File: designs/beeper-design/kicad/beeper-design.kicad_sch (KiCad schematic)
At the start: 90 parts, among them J1 TC2030-IDC-NL, J2 TC2030-IDC-NL, J3 2X1-pin-header, J4 2X1-pin-header, J5 6X1-pin-header, U1 DA14705-00000HZ2, U10 PMM-3738-VM1000-R, U11 LI0805H151R-10, U12 DRV2605YZFR, U13 CSD75207W15, U14 EVPBB4A9B000, U15 EVPBB4A9B000, U16 EVPBB4A9B000, U2 AT25FF321A-UUN-T, U3 BQ51003YFPR, U4 DA7212-01UM2, U5 PMM-3738-VM1000-R, U6 LI0805H151R-10, U7 PMM-3738-VM1000-R, U8 LI0805H151R-10, U9 LSM6DSOXTR, X1 ABM12-32.000MHZ-B2X-T3

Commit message: fixed BGA ball landpattern
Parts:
- removed C10: 2.2u, beeper-design:Pkg0201_4, symbol my_capacitor_35
- removed C11: 10u, beeper-design:Pkg0402_1, symbol my_capacitor
- removed C12: 10u, beeper-design:Pkg0402_1, symbol my_capacitor_18
- removed C13: 1u, beeper-design:Pkg0201_4, symbol my_capacitor_4
- removed C14: 2.2u, beeper-design:Pkg0201_4, symbol my_capacitor_33
- removed C15: 470n, beeper-design:Pkg0201_4, symbol my_capacitor_37
- removed C16: 470n, beeper-design:Pkg0201_4, symbol my_capacitor_41
- removed C17: 22n, beeper-design:Pkg0201_1, symbol my_capacitor_3
- removed C18: 22n, beeper-design:Pkg0201_1, symbol my_capacitor_6
- removed C19: 10n, beeper-design:Pkg0201_1, symbol my_capacitor_10
- removed C2: 22u, beeper-design:Pkg0603, symbol my_capacitor_24
- removed C20: 10n, beeper-design:Pkg0201_1, symbol my_capacitor_16
- removed C21: 270p, beeper-design:Pkg0201_1, symbol my_capacitor_20
- removed C22: 10n, beeper-design:Pkg0201_1, symbol my_capacitor_25
- removed C23: 10u, beeper-design:Pkg0402_1, symbol my_capacitor_36
- removed C24: 4.7u, beeper-design:Pkg0402_2, symbol my_capacitor_40
- removed C25: 4.7u, beeper-design:Pkg0402_2, symbol my_capacitor_29
- removed C26: 1u, beeper-design:Pkg0201_4, symbol my_capacitor_26
- removed C27: 100n, beeper-design:Pkg0201_1, symbol my_capacitor_34
- removed C28: 1u, beeper-design:Pkg0201_4, symbol my_capacitor_39
- removed C29: 1u, beeper-design:Pkg0201_4, symbol my_capacitor_1
- removed C3: 22u, beeper-design:Pkg0603, symbol my_capacitor_32
- removed C30: 1u, beeper-design:Pkg0201_4, symbol my_capacitor_5
- removed C31: 1u, beeper-design:Pkg0201_4, symbol my_capacitor_7
- removed C32: 1u, beeper-design:Pkg0201_4, symbol my_capacitor_11
- removed C33: 1u, beeper-design:Pkg0201_4, symbol my_capacitor_17
- removed C34: 1u, beeper-design:Pkg0201_4, symbol my_capacitor_22
- removed C35: 1u, beeper-design:Pkg0201_4, symbol my_capacitor_28
- removed C36, C39, C44: 1u, beeper-design:Pkg0201_4, symbol my_capacitor_13
- removed C37, C40, C45: 100p, beeper-design:Pkg0201_1, symbol my_capacitor_19
- removed C38, C41, C46: 1u, beeper-design:Pkg0201_4, symbol my_capacitor_31
- removed C4: 47u, beeper-design:Pkg0805_1, symbol my_capacitor_38
- removed C42: 100n, beeper-design:Pkg0201_1, symbol my_capacitor_9
- removed C43: 100n, beeper-design:Pkg0201_1, symbol my_capacitor_14
- removed C47: 1u, beeper-design:Pkg0201_4, symbol my_capacitor_23
- removed C48: 1u, beeper-design:Pkg0201_4, symbol my_capacitor_30
- removed C5: 100n, beeper-design:Pkg0201_1, symbol my_capacitor_2
- removed C6: 47u, beeper-design:Pkg0805_1, symbol my_capacitor_8
- removed C7: 10u, beeper-design:Pkg0402_1, symbol my_capacitor_12
- removed C8: 10u, beeper-design:Pkg0402_1, symbol my_capacitor_21
- removed C9: 10u, beeper-design:Pkg0402_1, symbol my_capacitor_27
- removed J1, J2: TC2030-IDC-NL, beeper-design:TC2030_IDC_NL_FOOTPRINT, symbol component_1
- removed J3, J4: 2X1-pin-header, beeper-design:PIN_GRID_1, symbol pin_header
- removed J5: 6X1-pin-header, beeper-design:PIN_GRID, symbol pin_header_1
- removed R1: 0R, beeper-design:Pkg0201_5, symbol my_resistor_9
- removed R10, R11, R9: 47K, beeper-design:Pkg0201_5, symbol my_resistor_7
- removed R12, R13: 8K2, beeper-design:Pkg0201_5, symbol my_resistor_1
- removed R14, R15: 8K2, beeper-design:Pkg0201_5, symbol my_resistor_5
- removed R16, R17: 8K2, beeper-design:Pkg0201_5, symbol my_resistor_11
- removed R2: 845R, beeper-design:Pkg0201_5, symbol my_resistor_10
- removed R3: 196R, beeper-design:Pkg0201, symbol my_resistor
- removed R4: 20K, beeper-design:Pkg0201_3, symbol my_resistor_2
- removed R5: 10K, beeper-design:Pkg0201_5, symbol my_resistor_3
- removed R6: 10K, beeper-design:Pkg0201_5, symbol my_resistor_4
- removed R7: 10K, beeper-design:Pkg0201_5, symbol my_resistor_6
- removed R8: 1K, beeper-design:Pkg0201, symbol my_resistor_8
- removed U10, U5, U7: PMM-3738-VM1000-R, beeper-design:LP_7, symbol PMM_3738_VM1000_R
- removed U11, U6, U8: LI0805H151R-10, beeper-design:Pkg0805, symbol component
- removed U4: DA7212-01UM2, beeper-design:LP_2, symbol component_2
- removed X1: ABM12-32.000MHZ-B2X-T3, beeper-design:XTAL_TSX_3225, symbol component_3
- added C10: 2.2u, beeper-design:Pkg0201_4, symbol my_capacitor_32
- added C11: 10u, beeper-design:Pkg0402_1, symbol my_capacitor_38
- added C12: 10u, beeper-design:Pkg0402_1, symbol my_capacitor_19
- added C13: 1u, beeper-design:Pkg0201_4, symbol my_capacitor_24
- added C14: 2.2u, beeper-design:Pkg0201_4, symbol my_capacitor_8
- added C15: 470n, beeper-design:Pkg0201_4, symbol my_capacitor_12
- added C16: 470n, beeper-design:Pkg0201_4, symbol my_capacitor_18
- added C17: 22n, beeper-design:Pkg0201_1, symbol my_capacitor_23
- added C18: 22n, beeper-design:Pkg0201_1, symbol my_capacitor_29
- added C19: 10n, beeper-design:Pkg0201_1, symbol my_capacitor_33
- added C2: 22u, beeper-design:Pkg0603, symbol my_capacitor_27
- added C20: 10n, beeper-design:Pkg0201_1, symbol my_capacitor_37
- added C21: 270p, beeper-design:Pkg0201_1, symbol my_capacitor_1
- added C22: 10n, beeper-design:Pkg0201_1, symbol my_capacitor_3
- added C23: 10u, beeper-design:Pkg0402_1, symbol my_capacitor_10
- added C24: 4.7u, beeper-design:Pkg0402_2, symbol my_capacitor_16
- added C25: 4.7u, beeper-design:Pkg0402_2, symbol my_capacitor_6
- added C26: 1u, beeper-design:Pkg0201_4, symbol my_capacitor_4
- added C27: 100n, beeper-design:Pkg0201_1, symbol my_capacitor_9
- added C28: 1u, beeper-design:Pkg0201_4, symbol my_capacitor_14
- added C29: 1u, beeper-design:Pkg0201_4, symbol my_capacitor_20
- added C3: 22u, beeper-design:Pkg0603, symbol my_capacitor_31
- added C30: 1u, beeper-design:Pkg0201_4, symbol my_capacitor_25
- added C31: 1u, beeper-design:Pkg0201_4, symbol my_capacitor_30
- added C32: 1u, beeper-design:Pkg0201_4, symbol my_capacitor_34
- added C33: 1u, beeper-design:Pkg0201_4, symbol my_capacitor_39
- added C34: 1u, beeper-design:Pkg0201_4, symbol my_capacitor_2
- added C35: 1u, beeper-design:Pkg0201_4, symbol my_capacitor_5
- added C36: 100n, beeper-design:Pkg0201_1, symbol my_capacitor_40
- added C4: 47u, beeper-design:Pkg0805, symbol my_capacitor_35
- added C42: 100n, beeper-design:Pkg0201_1, symbol my_capacitor_21
- added C43: 100n, beeper-design:Pkg0201_1, symbol my_capacitor_26
- added C47: 1u, beeper-design:Pkg0201_4, symbol my_capacitor_11
- added C48: 1u, beeper-design:Pkg0201_4, symbol my_capacitor_17
- added C49: 1p, beeper-design:Pkg0201_1, symbol my_capacitor_36
- added C5: 100n, beeper-design:Pkg0201_1, symbol my_capacitor
- added C50: 1p, beeper-design:Pkg0201_1, symbol my_capacitor_41
- added C6: 47u, beeper-design:Pkg0805, symbol my_capacitor_7
- added C7: 10u, beeper-design:Pkg0402_1, symbol my_capacitor_13
- added C8: 10u, beeper-design:Pkg0402_1, symbol my_capacitor_22
- added C9: 10u, beeper-design:Pkg0402_1, symbol my_capacitor_28
- added F1: TPD4S012DRYR, beeper-design:SON_6_L1_5_W1_0_P0_50_BL, symbol C96506
- added J1: TC2030-IDC-NL, beeper-design:TC2030_IDC_NL_FOOTPRINT, symbol component_2
- added J3, J4: 2X1-pin-header, beeper-design:PIN_GRID_1, symbol pin_header_1
- added J5: 6X1-pin-header, beeper-design:PIN_GRID, symbol pin_header
- added J6: 10103594-0001LF, beeper-design:AMPHENOL_10103594_0001LF, symbol AMPHENOL_10103594_0001LF
- added L3: 1n, beeper-design:Pkg0201_2, symbol my_inductor_2
- added R1: 0R, beeper-design:Pkg0201_5, symbol my_resistor_8
- added R12, R13: 8K2, beeper-design:Pkg0201_5, symbol my_resistor_7
- added R14, R15: 8K2, beeper-design:Pkg0201_5, symbol my_resistor_2
- added R16, R17: 8K2, beeper-design:Pkg0201_5, symbol my_resistor_5
- added R18: 100K, beeper-design:Pkg0201_5, symbol my_resistor_10
- added R2: 845R, beeper-design:Pkg0201_5, symbol my_resistor_3
- added R3: 196R, beeper-design:Pkg0201, symbol my_resistor_4
- added R4: 20K, beeper-design:Pkg0201_3, symbol my_resistor_6
- added R5: 10K, beeper-design:Pkg0201_5, symbol my_resistor_9
- added R6: 10K, beeper-design:Pkg0201_5, symbol my_resistor_11
- added R7: 10K, beeper-design:Pkg0201_5, symbol my_resistor
- added R8: 1K, beeper-design:Pkg0201, symbol my_resistor_1
- added U17: (no value), beeper-design:Pkg_2450AT18D0100_STD_R_1, symbol component_1
- added U4: DA7212-01UM2, beeper-design:LP, symbol component
- added XTAL1: XRCGB32M000F1H00R0, beeper-design:CRYSTAL_SMD_4P_L2_0_W1_6_BL_1, symbol C880116
- U1: footprint beeper-design:LP_1 -> beeper-design:LP_5
- U12: footprint beeper-design:LP_5 -> beeper-design:LP_6
- U14, U15, U16: footprint beeper-design:LP_6 -> beeper-design:LP_2
- U9: footprint beeper-design:LP -> beeper-design:LP_1
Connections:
- net GND: now also C10.1, C11.1, C12.1, C13.1, C14.1, C2.1, C23.1, C24.1, C25.1, C26.1, C27.1, C28.1, C29.1, C3.1, C30.1, C31.1, C32.1, C33.1, C34.1, C36.2, C4.1, C42.1, C43.1, C47.1, C48.1, C49.2, C5.1, C50.2, C6.1, C7.1, C8.1, C9.1, F1.4 (GND), J1.5, J5.6, J6.5 (GND), R18.2, R3.2, R5.2, R6.2, R7.2, R8.2, U17.0 (GND), U17.2 (GND), U17.3 (GND), U4.B10 (GND_A), U4.B2 (GND_CP), XTAL1.2 (GND1), XTAL1.4 (GND0)
- net OUT+: now also J4.1
- net OUT-: now also J4.2
- net VDD1P4: now also C2.2, C3.2
- net VDD1P8: now also C26.2, C28.2, C32.2, C4.2, C42.2, C43.2, U4.B14 (VDD_MIC), U4.B6 (VDD_A), U4.D10 (VDD_IO)
- net VDD1P8F: now also C5.2, R1.1
- net VDD1P8P: now also C6.2, R1.2
- net VDD3P0: now also C7.2
- net VDDBAT: now also C8.2
- net VDDBUS: now also C9.2
- net VLED: now also C10.2
- net codec-i2c_sda: now also U1.H12 (P2_08), R12.1, U4.C9 (SDA); no longer U1.D2 (P2_12)
- net drv-i2c_sda: now also U1.A5 (P2_07), R16.1; no longer U1.G1 (P2_11)
- net mcu-but0_gpio: now also U1.B1 (P2_04); no longer U1.H12 (P2_08)
- net mcu-but1_gpio: now also U1.B2 (P2_05); no longer U1.H11 (P2_09)
- net mcu-but2_gpio: now also U1.A4 (P2_06); no longer U1.F1 (P2_10)
- net mcu-hap0_gpio: now also U1.F2 (P1_28); no longer U1.E4 (P2_02)
- net mcu-hap1_gpio: now also U1.D1 (P1_29); no longer U1.E6 (P2_03)
- net mcu-wpwr0_gpio: now also U1.E3 (P2_00), R5.1; no longer U1.B1 (P2_04)
- net mcu-wpwr1_gpio: now also U1.J9 (P2_01), R6.1; no longer U1.B2 (P2_05)
- net mcu-wpwr2_gpio: now also U1.E4 (P2_02); no longer U1.A4 (P2_06)
- net mcu-wpwr3_gpio: now also U1.E6 (P2_03), R7.1; no longer U1.A5 (P2_07)
- net mcu_dbg-m33_swdclk: now also J1.4
- net mcu_mcu-etm_clk: now also J5.1
- net mcu_mcu-etm_data0: now also J5.2
- net mcu_mcu-etm_data1: now also J5.3
- net mcu_mcu-etm_data2: now also J5.4
- net mcu_mcu-etm_data3: now also J5.5
- net at U3.G4 (AD): now also R8.1
- net at U3.B1 (AC2), U3.B2 (AC2): now also C16.1, C18.1, C20.1, C21.1, J3.2
- net at U3.F2 (FOD): now also R2.2, R3.1, R4.1
- net at U3.C2 (RECT), U3.C3 (RECT): now also C23.2, C24.2, R4.2
- net at U3.B3 (AC1), U3.B4 (AC1): now also C15.1, C17.1, C19.1, C21.2, C22.2
- net at U1.A10 (RFIOP): now also C49.1, L3.1
- net at U1.F11 (XTAL32Mp): now also XTAL1.1
- net at U1.F12 (XTAL32Mm): now also XTAL1.3
- net at U3.E4 (COMM1): now also C17.2
- net at U12.A2 (REG): now also C47.2
- net at U3.G1 (ILIM): now also R2.1
- net VBUS: now reaches U13.A1 (G1), U13.A2 (D10), U13.A3 (D11)
- net VBUS: now also C25.2, F1.6 (VBUS), J6.1 (VCC)
- net at U3.E2 (CLAMP2): now also C16.2
- net at U3.C1 (BOOT2): now also C20.2
- net at U3.C4 (BOOT1): now also C19.2
- net at U3.E1 (COMM2): now also C18.2
- net at U3.E3 (CLAMP1): now also C15.2
- net VAD: no longer names the net of U1.M9 (VAD)
- net VSYS renamed VDDSYS
- net VDDSYS: now also C11.2, C12.2, C13.2, C14.2, C29.2, C48.2, J1.1, R12.2, R13.2, R14.2, R15.2, R16.2, R17.2, U4.A11 (VDD_SP)
- net codec-i2c_scl renamed mcu_conn-uart_tx
- net mcu_conn-uart_tx: now also J1.6
- net drv-i2c_scl renamed mcu-hap-i2c_scl
- net mcu-hap-i2c_scl: now also U1.H11 (P2_09), R17.1; no longer U1.D3 (P2_13)
- net mcu-i3c_sda renamed qsen-i3c_sda
- net qsen-i3c_sda: now also R14.1
- net mcu_conn-reset_reset: no longer names the net of U1.B10 (nRST)
- net mcu_dbg-m33_swdio renamed mcu_mcu-dbg-m33_swdio
- net mcu_mcu-dbg-m33_swdio: now also J1.2
- net mcu_dbg-snc_swdclk: no longer names the net of U1.D7 (P0_03)
- net mcu_dbg-snc_swdio: no longer names the net of U1.D8 (P0_02)
- net qsen-i3c_scl renamed mcu-i3c_scl
- net mcu-i3c_scl: now also R15.1
- new net: C22.1, J3.1
- new net: C50.1, L3.2, U17.1
- new net: C33.2, U4.A1 (HPCSP)
- new net: C31.2, U4.A7 (DACREF)
- new net: C30.2, U4.A9 (VMID)
- new net: C35.1, U4.C1 (HPCSN)
- new net: C35.2, U4.C3 (HPCFN)
- new net: C27.2, U4.D12 (VDIG)
- new net: C34.2, U4.D2 (HPCFP)
- new net D+: F1.1 (D+), J6.3 (D+), U1.F1 (P2_10)
- new net D-: F1.2 (D-), J6.2 (D-), U1.G1 (P2_11)
- new net SHIELD: C36.1, J6.10 (SHIELD), J6.11 (SHIELD), J6.13 (SHIELD), J6.14 (SHIELD), J6.6 (SHIELD), J6.7 (SHIELD), J6.8 (SHIELD), J6.9 (SHIELD), R18.1
- new net mcu-codec-i2c_scl: R13.1, U1.D2 (P2_12), U4.D8 (SCL)
- new net mcu_mcu-uart_rx: J1.3, U1.D3 (P2_13)
- no-connect marks 8 -> 9

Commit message: fixed up 3D flex conn
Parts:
- removed C1: 22u, beeper-design:Pkg0603, symbol my_capacitor_15
- removed C10: 2.2u, beeper-design:Pkg0201_4, symbol my_capacitor_32
- removed C11: 10u, beeper-design:Pkg0402_1, symbol my_capacitor_38
- removed C12: 10u, beeper-design:Pkg0402_1, symbol my_capacitor_19
- removed C13: 1u, beeper-design:Pkg0201_4, symbol my_capacitor_24
- removed C14: 2.2u, beeper-design:Pkg0201_4, symbol my_capacitor_8
- removed C15: 470n, beeper-design:Pkg0201_4, symbol my_capacitor_12
- removed C16: 470n, beeper-design:Pkg0201_4, symbol my_capacitor_18
- removed C17: 22n, beeper-design:Pkg0201_1, symbol my_capacitor_23
- removed C18: 22n, beeper-design:Pkg0201_1, symbol my_capacitor_29
- removed C19: 10n, beeper-design:Pkg0201_1, symbol my_capacitor_33
- removed C2: 22u, beeper-design:Pkg0603, symbol my_capacitor_27
- removed C20: 10n, beeper-design:Pkg0201_1, symbol my_capacitor_37
- removed C21: 270p, beeper-design:Pkg0201_1, symbol my_capacitor_1
- removed C22: 10n, beeper-design:Pkg0201_1, symbol my_capacitor_3
- removed C23: 10u, beeper-design:Pkg0402_1, symbol my_capacitor_10
- removed C24: 4.7u, beeper-design:Pkg0402_2, symbol my_capacitor_16
- removed C25: 4.7u, beeper-design:Pkg0402_2, symbol my_capacitor_6
- removed C26: 1u, beeper-design:Pkg0201_4, symbol my_capacitor_4
- removed C27: 100n, beeper-design:Pkg0201_1, symbol my_capacitor_9
- removed C28: 1u, beeper-design:Pkg0201_4, symbol my_capacitor_14
- removed C29: 1u, beeper-design:Pkg0201_4, symbol my_capacitor_20
- removed C3: 22u, beeper-design:Pkg0603, symbol my_capacitor_31
- removed C30: 1u, beeper-design:Pkg0201_4, symbol my_capacitor_25
- removed C31: 1u, beeper-design:Pkg0201_4, symbol my_capacitor_30
- removed C32: 1u, beeper-design:Pkg0201_4, symbol my_capacitor_34
- removed C33: 1u, beeper-design:Pkg0201_4, symbol my_capacitor_39
- removed C34: 1u, beeper-design:Pkg0201_4, symbol my_capacitor_2
- removed C35: 1u, beeper-design:Pkg0201_4, symbol my_capacitor_5
- removed C36: 100n, beeper-design:Pkg0201_1, symbol my_capacitor_40
- removed C4: 47u, beeper-design:Pkg0805, symbol my_capacitor_35
- removed C42: 100n, beeper-design:Pkg0201_1, symbol my_capacitor_21
- removed C43: 100n, beeper-design:Pkg0201_1, symbol my_capacitor_26
- removed C47: 1u, beeper-design:Pkg0201_4, symbol my_capacitor_11
- removed C48: 1u, beeper-design:Pkg0201_4, symbol my_capacitor_17
- removed C49: 1p, beeper-design:Pkg0201_1, symbol my_capacitor_36
- removed C5: 100n, beeper-design:Pkg0201_1, symbol my_capacitor
- removed C50: 1p, beeper-design:Pkg0201_1, symbol my_capacitor_41
- removed C6: 47u, beeper-design:Pkg0805, symbol my_capacitor_7
- removed C7: 10u, beeper-design:Pkg0402_1, symbol my_capacitor_13
- removed C8: 10u, beeper-design:Pkg0402_1, symbol my_capacitor_22
- removed C9: 10u, beeper-design:Pkg0402_1, symbol my_capacitor_28
- removed F1: TPD4S012DRYR, beeper-design:SON_6_L1_5_W1_0_P0_50_BL, symbol C96506
- removed J1: TC2030-IDC-NL, beeper-design:TC2030_IDC_NL_FOOTPRINT, symbol component_2
- removed J3, J4: 2X1-pin-header, beeper-design:PIN_GRID_1, symbol pin_header_1
- removed J5: 6X1-pin-header, beeper-design:PIN_GRID, symbol pin_header
- removed J6: 10103594-0001LF, beeper-design:AMPHENOL_10103594_0001LF, symbol AMPHENOL_10103594_0001LF
- removed L1: 470n, beeper-design:Pkg0201_2, symbol my_inductor
- removed L2: 1u, beeper-design:Pkg0402, symbol my_inductor_1
- removed L3: 1n, beeper-design:Pkg0201_2, symbol my_inductor_2
- removed LED1: TJ-S1615SW6TWMLCCYRGB-A5, beeper-design:LED_SMD_4P_L1_6_W1_5_TJ_S1615SW6TWMLCCYRGB_A5, symbol C601682
- removed R1: 0R, beeper-design:Pkg0201_5, symbol my_resistor_8
- removed R12, R13: 8K2, beeper-design:Pkg0201_5, symbol my_resistor_7
- removed R14, R15: 8K2, beeper-design:Pkg0201_5, symbol my_resistor_2
- removed R16, R17: 8K2, beeper-design:Pkg0201_5, symbol my_resistor_5
- removed R18: 100K, beeper-design:Pkg0201_5, symbol my_resistor_10
- removed R2: 845R, beeper-design:Pkg0201_5, symbol my_resistor_3
- removed R3: 196R, beeper-design:Pkg0201, symbol my_resistor_4
- removed R4: 20K, beeper-design:Pkg0201_3, symbol my_resistor_6
- removed R5: 10K, beeper-design:Pkg0201_5, symbol my_resistor_9
- removed R6: 10K, beeper-design:Pkg0201_5, symbol my_resistor_11
- removed R7: 10K, beeper-design:Pkg0201_5, symbol my_resistor
- removed R8: 1K, beeper-design:Pkg0201, symbol my_resistor_1
- removed U1: DA14705-00000HZ2, beeper-design:LP_5, symbol DA14705
- removed U12: DRV2605YZFR, beeper-design:LP_6, symbol DRV2605YZFR
- removed U13: CSD75207W15, beeper-design:LP_3, symbol CSD75207W15
- removed U14, U15, U16: EVPBB4A9B000, beeper-design:LP_2, symbol C140848
- removed U17: (no value), beeper-design:Pkg_2450AT18D0100_STD_R_1, symbol component_1
- removed U2: AT25FF321A-UUN-T, beeper-design:WLCSP_12, symbol AT25FF321A_UUN_T
- removed U3: BQ51003YFPR, beeper-design:LP_4, symbol BQ51003YFPR
- removed U4: DA7212-01UM2, beeper-design:LP, symbol component
- removed U9: LSM6DSOXTR, beeper-design:LP_1, symbol LSM6DSOXTR
- removed XTAL1: XRCGB32M000F1H00R0, beeper-design:CRYSTAL_SMD_4P_L2_0_W1_6_BL_1, symbol C880116
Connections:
- no-connect marks 9 -> 0
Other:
- added sheet board-io flex-conn.beeper-connector haptic.board-io.hapdrv.rs.collector (beeper-design-3.kicad_sch)
- added sheet mcu usb.mcu.usb.micro-usb (beeper-design-4.kicad_sch)
- added sheet wpwr.module (beeper-design-2.kicad_sch)

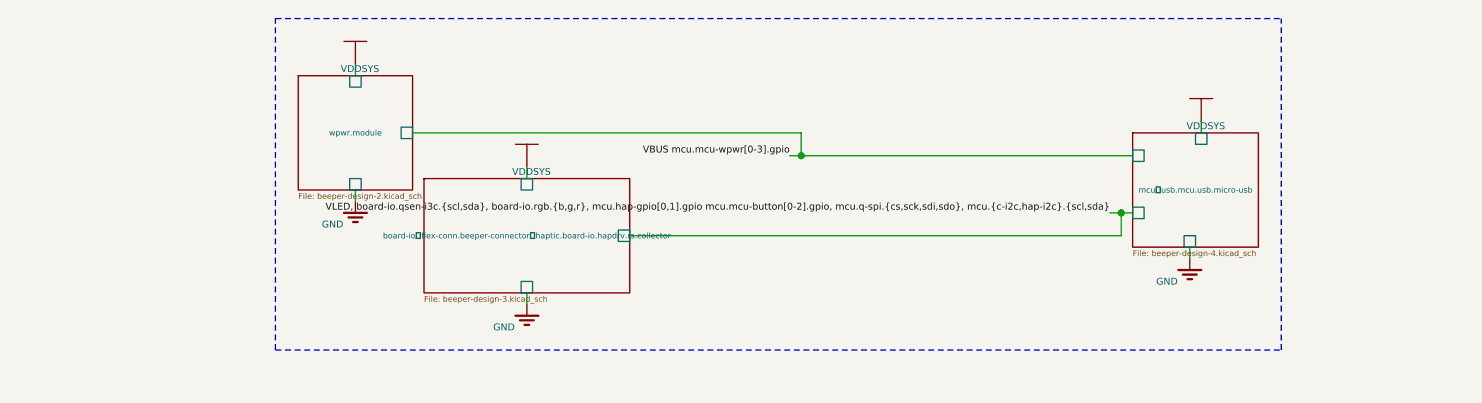
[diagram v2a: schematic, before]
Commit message: better export + JLCPCB numbers
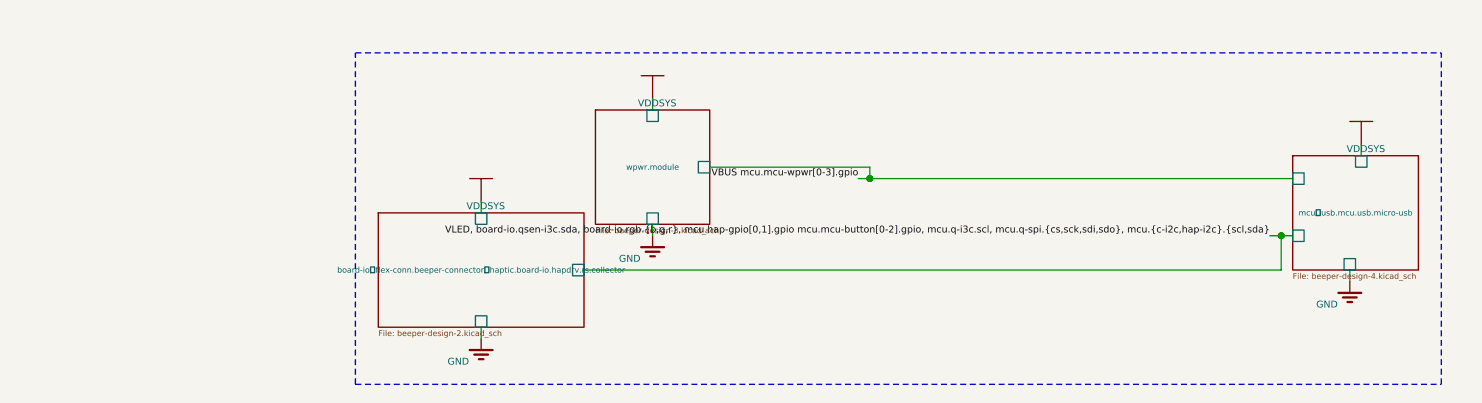
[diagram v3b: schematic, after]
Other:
- sheet board-io flex-conn.beeper-connector haptic.board-io.hapdrv.rs.collector: file beeper-design-3.kicad_sch -> beeper-design-2.kicad_sch
- sheet wpwr.module: file beeper-design-2.kicad_sch -> beeper-design-3.kicad_sch

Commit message: post export, had to munge sch
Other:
- removed sheet board-io flex-conn.beeper-connector haptic.board-io.hapdrv.rs.collector
- removed sheet mcu usb.mcu.usb.micro-usb
- removed sheet wpwr.module
- added sheet board-io (beeper-design-6.kicad_sch)
- added sheet board-io.hapdrv (beeper-design-4.kicad_sch)
- added sheet flex-conn.beeper-connector wpwr.module (beeper-design-5.kicad_sch)
- added sheet mcu (beeper-design-3.kicad_sch)
- added sheet mcu.mem.module (beeper-design-2.kicad_sch)

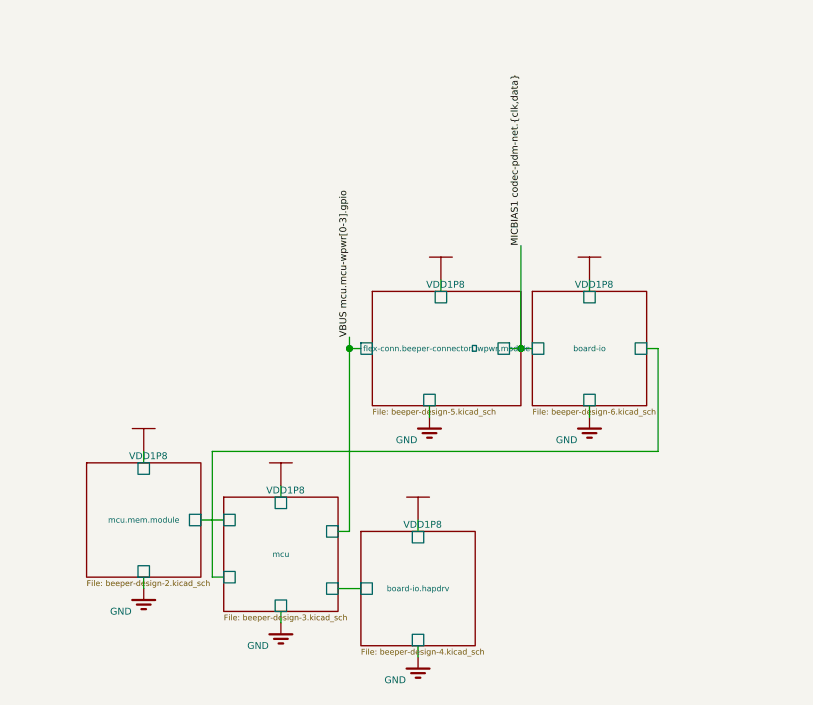
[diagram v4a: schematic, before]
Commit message: fixing drc errors
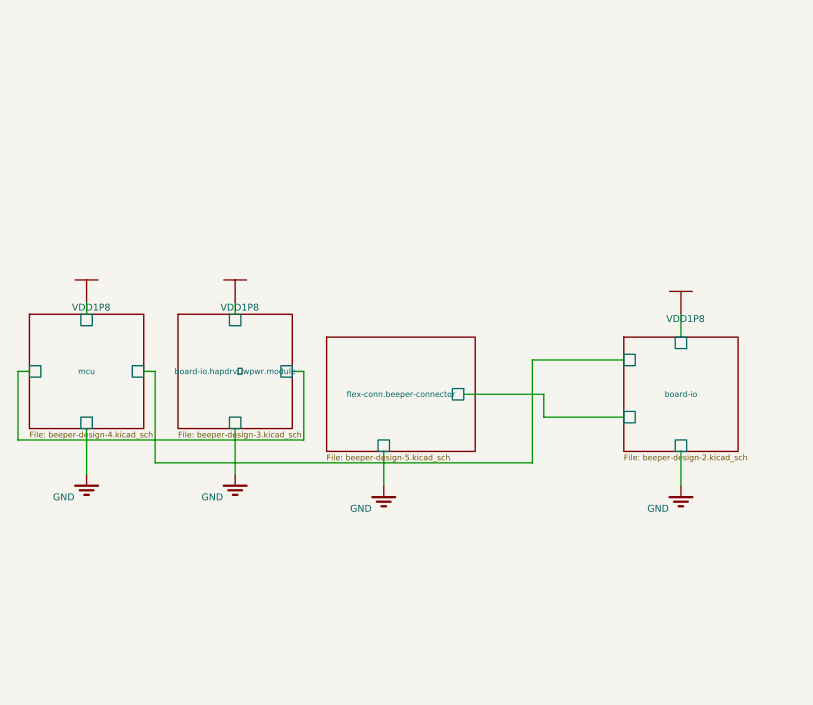
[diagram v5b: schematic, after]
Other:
- removed sheet board-io.hapdrv
- removed sheet flex-conn.beeper-connector wpwr.module
- removed sheet mcu.mem.module
- added sheet board-io.hapdrv wpwr.module (beeper-design-3.kicad_sch)
- added sheet flex-conn.beeper-connector (beeper-design-5.kicad_sch)
- sheet board-io: file beeper-design-6.kicad_sch -> beeper-design-2.kicad_sch
- sheet mcu: file beeper-design-3.kicad_sch -> beeper-design-4.kicad_sch

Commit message: updated kicad export
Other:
- sheet board-io: file beeper-design-2.kicad_sch -> beeper-design-3.kicad_sch
- sheet board-io.hapdrv wpwr.module: file beeper-design-3.kicad_sch -> beeper-design-4.kicad_sch
- sheet flex-conn.beeper-connector: file beeper-design-5.kicad_sch -> beeper-design-2.kicad_sch
- sheet mcu: file beeper-design-4.kicad_sch -> beeper-design-5.kicad_sch

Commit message: exported yet again
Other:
- sheet board-io: file beeper-design-3.kicad_sch -> beeper-design-2.kicad_sch
- sheet board-io.hapdrv wpwr.module: file beeper-design-4.kicad_sch -> beeper-design-3.kicad_sch
- sheet flex-conn.beeper-connector: file beeper-design-2.kicad_sch -> beeper-design-5.kicad_sch
- sheet mcu: file beeper-design-5.kicad_sch -> beeper-design-4.kicad_sch
